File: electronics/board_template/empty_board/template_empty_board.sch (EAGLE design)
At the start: 8 parts, among them IC1 L7805CD2T-TR, J1 GROVE_CONNECTOR2.0_1X4, J2 GROVE_CONNECTOR2.0_1X4

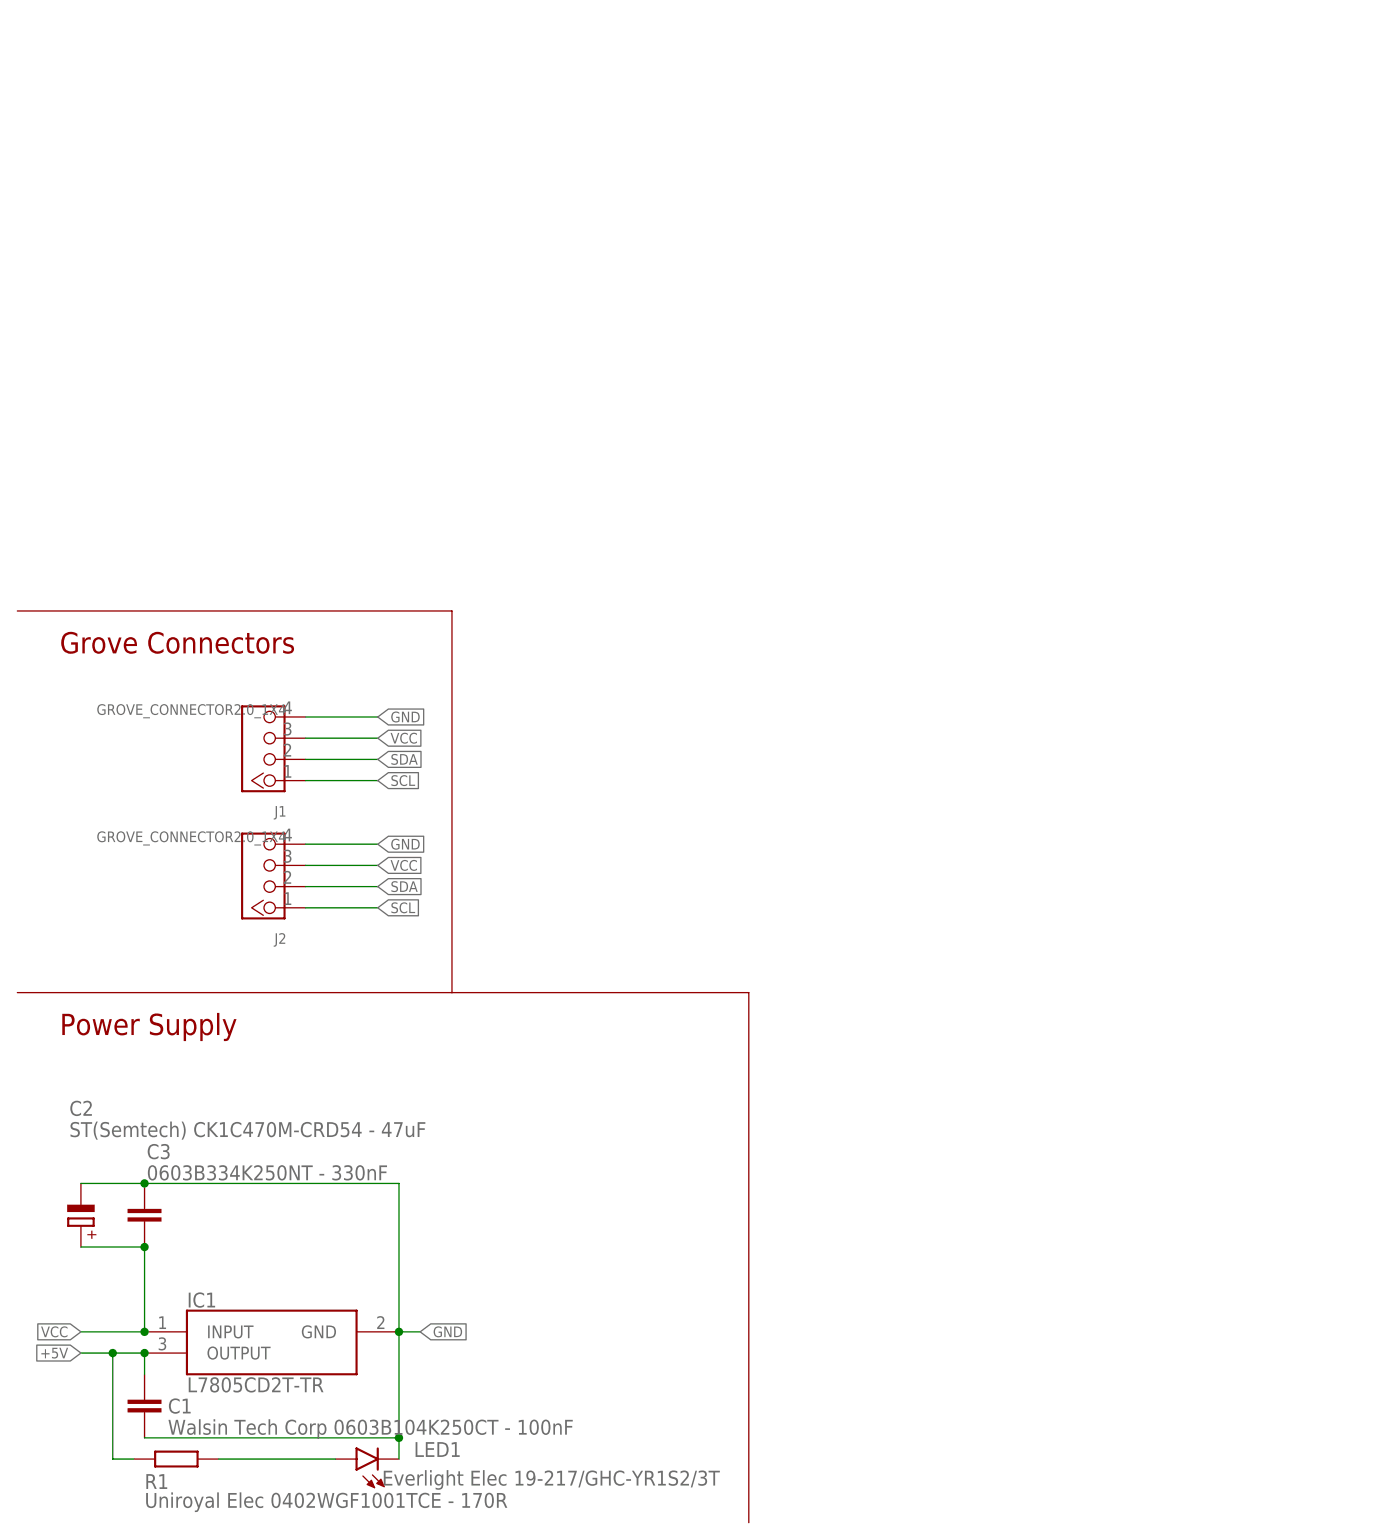
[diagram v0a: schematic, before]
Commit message: Template Empty Board an anderen Linearregler angepasst
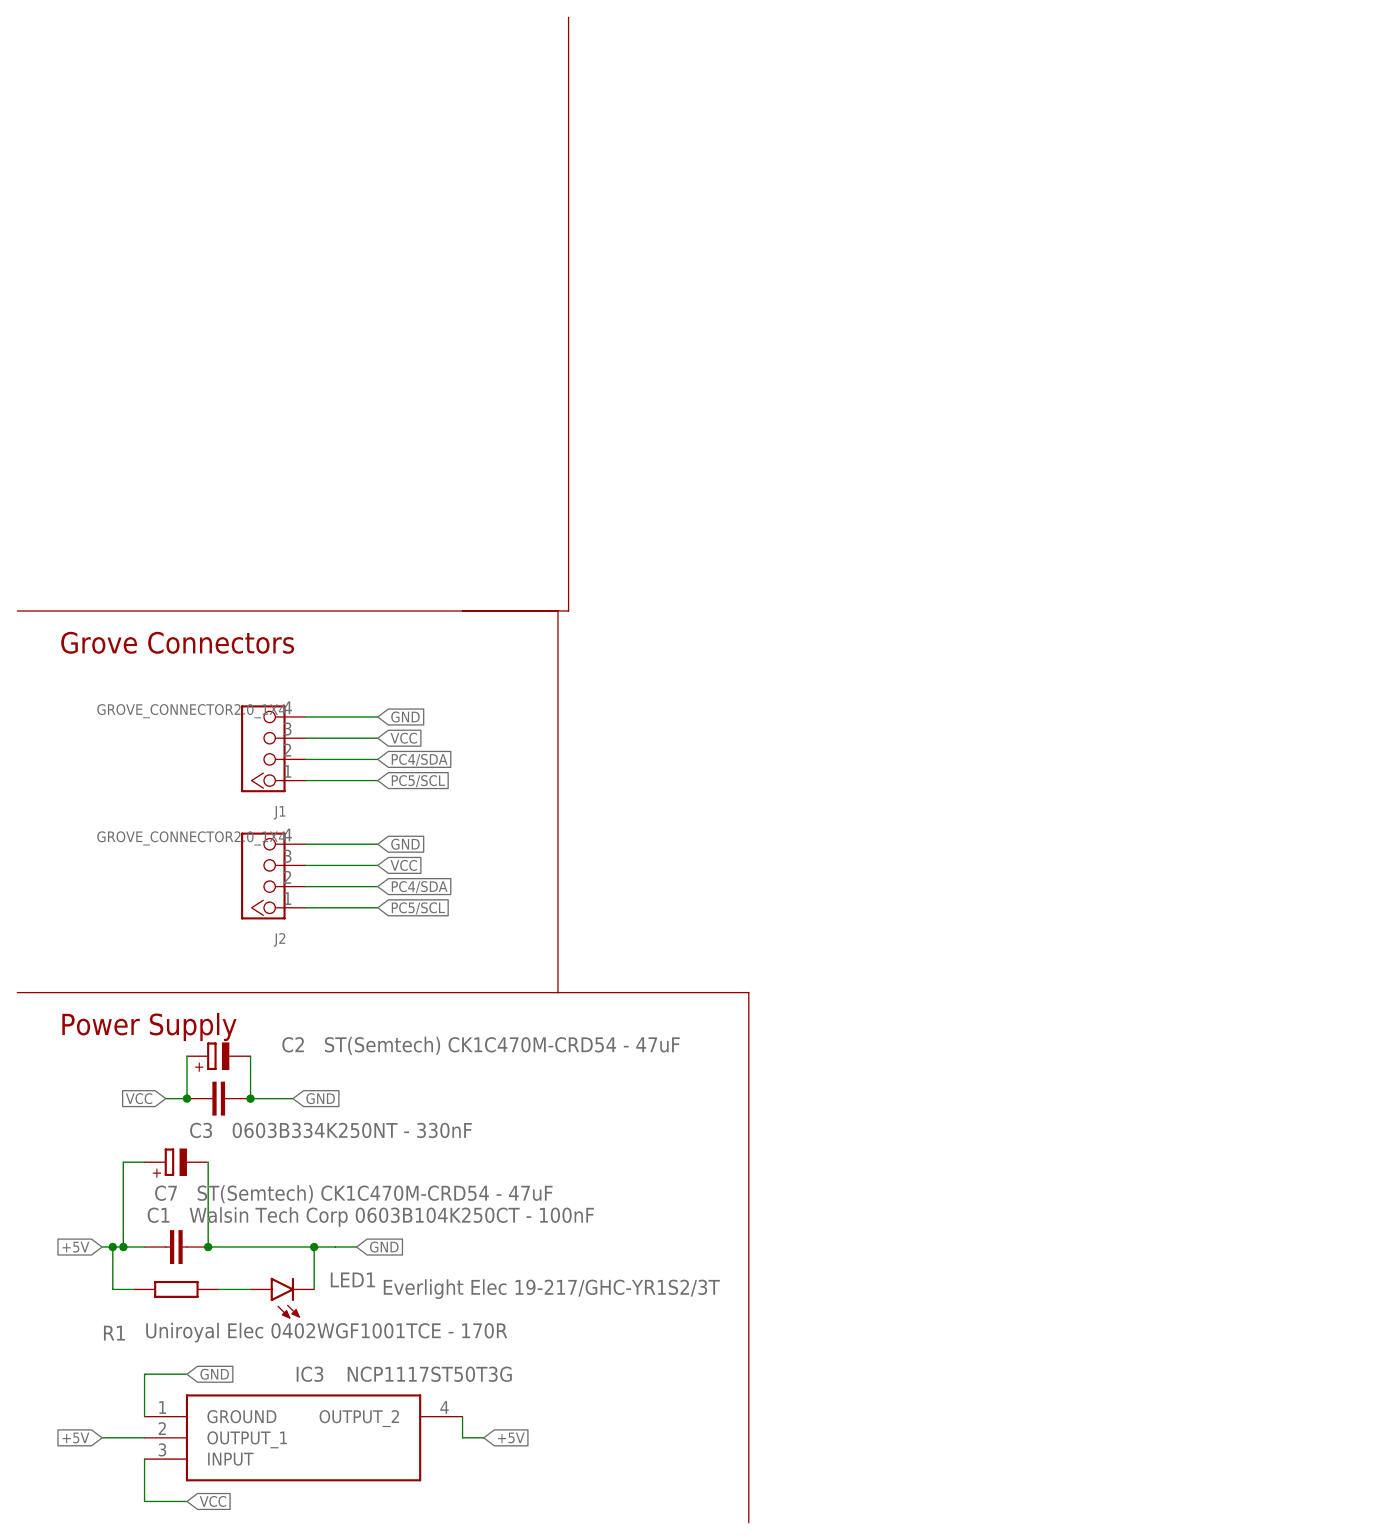
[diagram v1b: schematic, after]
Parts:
- removed IC1: L7805CD2T-TR, morphbot:L7805CD2T-TR
- added C7: ST(Semtech) CK1C470M-CRD54 - 47uF, rcl:CPOL-EUC
- added IC3: NCP1117ST50T3G, samacsys:NCP1117ST50T3G
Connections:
- net SCL renamed PC5/SCL
- net SDA renamed PC4/SDA
- net +5V: now also C7.+, IC3.OUTPUT_1, IC3.OUTPUT_2; no longer IC1.OUTPUT
- net GND: now also C7.-, IC3.GROUND; no longer IC1.GND
- net VCC: now also IC3.INPUT; no longer IC1.INPUT
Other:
- moved on the sheet: C1, C2, C3, LED1, R1

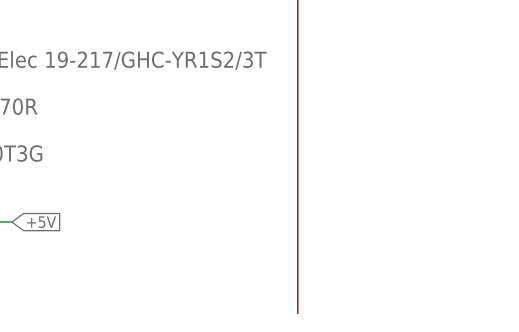
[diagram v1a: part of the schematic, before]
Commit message: Logo hinzugefügt
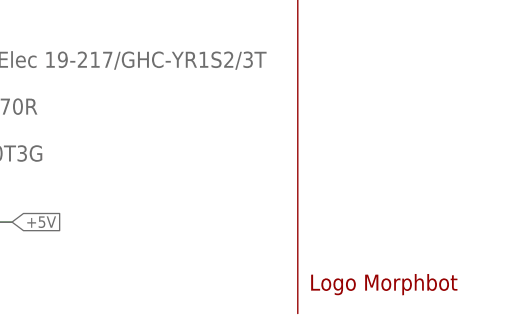
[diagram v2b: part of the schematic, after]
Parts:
- added U$1: LOGO_MORPHBOT5MM, topo-eng:LOGO_MORPHBOT5MM
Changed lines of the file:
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@@
 <layer number="104" name="Name" color="7" fill="1" visible="no" active="yes"/>
 <layer number="116" name="Patch_BOT" color="9" fill="4" visible="no" active="yes"/>
+<layer number="120" name="brd_placement_notes" color="7" fill="1" visible="yes" active="yes"/>
 <layer number="121" name="_tsilk" color="7" fill="1" visible="no" active="yes"/>
 <layer number="122" name="_bsilk" color="7" fill="1" visible="no" active="yes"/>
+<layer number="144" name="DrillLegend" color="7" fill="1" visible="yes" active="yes"/>
+<layer number="145" name="DrillLegend_01-16" color="7" fill="1" visible="yes" active="yes"/>
+<layer number="146" name="DrillLegend_01-20" color="7" fill="1" visible="yes" active="yes"/>
 <layer number="151" name="HeatSink" color="14" fill="1" visible="no" active="no"/>
+<layer number="198" name="BMP198" color="7" fill="1" visible="yes" active="yes"/>
+<layer number="199" name="Contour" color="7" fill="1" visible="yes" active="yes"/>
 <layer number="200" name="200bmp" color="1" fill="10" visible="no" active="no"/>
 <layer number="201" name="201bmp" color="2" fill="1" visible="no" active="no"/>
@@
 <layer number="207" name="207bmp" color="15" fill="10" visible="no" active="no"/>
 <layer number="208" name="208bmp" color="9" fill="10" visible="no" active="yes"/>
+<layer number="209" name="Route9Document" color="7" fill="1" visible="yes" active="yes"/>
+<layer number="210" name="Route10Document" color="7" fill="1" visible="yes" active="yes"/>
+<layer number="211" name="Route11Document" color="7" fill="1" visible="yes" active="yes"/>
+<layer number="212" name="Route12Document" color="7" fill="1" visible="yes" active="yes"/>
+<layer number="213" name="Route13Document" color="7" fill="1" visible="yes" active="yes"/>
+<layer number="214" name="Route14Document" color="7" fill="1" visible="yes" active="yes"/>
+<layer number="215" name="Route15Document" color="7" fill="1" visible="yes" active="yes"/>
+<layer number="216" name="BottomDocument" color="7" fill="1" visible="yes" active="yes"/>
+<layer number="220" name="DimensionDocument" color="7" fill="1" visible="yes" active="yes"/>
+<layer number="221" name="tPlaceDocument" color="7" fill="1" visible="yes" active="yes"/>
+<layer number="222" name="bPlaceDocument" color="7" fill="1" visible="yes" active="yes"/>
+<layer number="225" name="tNamesDocument" color="7" fill="1" visible="yes" active="yes"/>
+<layer number="226" name="bNamesDocument" color="7" fill="1" visible="yes" active="yes"/>
+<layer number="227" name="tValuesDocument" color="7" fill="1" visible="yes" active="yes"/>
+<layer number="228" name="bValuesDocument" color="7" fill="1" visible="yes" active="yes"/>
+<layer number="229" name="tStopDocument" color="7" fill="1" visible="yes" active="yes"/>
+<layer number="230" name="bStopDocument" color="7" fill="1" visible="yes" active="yes"/>
+<layer number="231" name="tCreamDocument" color="7" fill="1" visible="yes" active="yes"/>
+<layer number="232" name="bCreamDocument" color="7" fill="1" visible="yes" active="yes"/>
+<layer number="233" name="tFinishDocument" color="7" fill="1" visible="yes" active="yes"/>
+<layer number="234" name="bFinishDocument" color="7" fill="1" visible="yes" active="yes"/>
+<layer number="235" name="tGlueDocument" color="7" fill="1" visible="yes" active="yes"/>
+<layer number="236" name="bGlueDocument" color="7" fill="1" visible="yes" active="yes"/>
+<layer number="244" name="DrillsDocument" color="7" fill="1" visible="yes" active="yes"/>
+<layer number="245" name="HolesDocument" color="7" fill="1" visible="yes" active="yes"/>
+<layer number="246" name="MillingDocument" color="7" fill="1" visible="yes" active="yes"/>
+<layer number="247" name="MeasuresDocument" color="7" fill="1" visible="yes" active="yes"/>
 <layer number="250" name="Descript" color="3" fill="1" visible="no" active="no"/>
 <layer number="251" name="SMDround" color="12" fill="11" visible="no" active="no"/>
@@
 <part name="IC3" library="samacsys" deviceset="NCP1117ST50T3G" device=""/>
 <part name="C7" library="rcl" library_urn="urn:adsk.eagle:library:334" deviceset="CPOL-EU" device="C" package3d_urn="urn:adsk.eagle:package:23422/2" value="ST(Semtech) CK1C470M-CRD54 - 47uF"/>
+<part name="U$1" library="topo-eng" library_urn="urn:adsk.eagle:library:6646478" deviceset="LOGO_MORPHBOT" device="5MM"/>
 </parts>
 <sheets>
@@
 <attribute name="VALUE" x="21.463" y="38.5826" size="1.778" layer="96"/>
 </instance>
+<instance part="U$1" gate="G$1" x="88.9" y="2.54" smashed="yes"/>
 </instances>
 <busses>

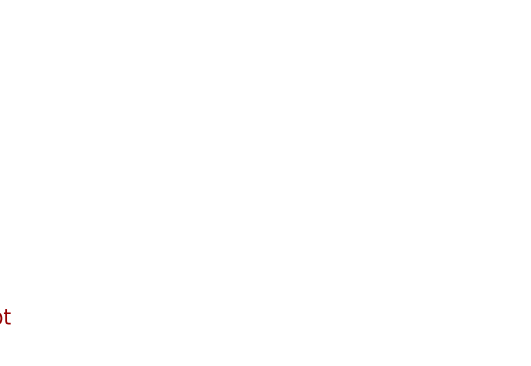
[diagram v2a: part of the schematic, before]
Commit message: Fiducials eingefügt
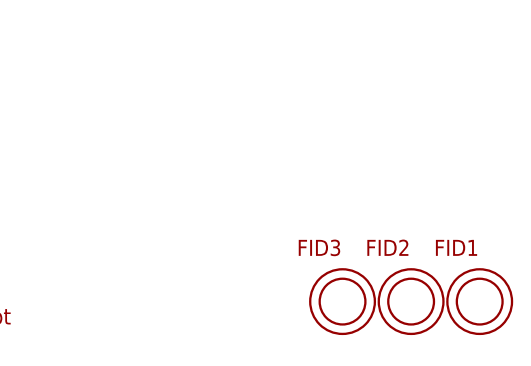
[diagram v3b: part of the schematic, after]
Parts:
- added FID1, FID2, FID3: OPEN-PNP-FIDUCIAL, topo-eng:OPEN-PNP-FIDUCIAL
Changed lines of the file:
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@@
 <part name="C7" library="rcl" library_urn="urn:adsk.eagle:library:334" deviceset="CPOL-EU" device="C" package3d_urn="urn:adsk.eagle:package:23422/2" value="ST(Semtech) CK1C470M-CRD54 - 47uF"/>
 <part name="U$1" library="topo-eng" library_urn="urn:adsk.eagle:library:6646478" deviceset="LOGO_MORPHBOT" device="5MM"/>
+<part name="FID1" library="topo-eng" library_urn="urn:adsk.eagle:library:6646478" deviceset="OPEN-PNP-FIDUCIAL" device=""/>
+<part name="FID2" library="topo-eng" library_urn="urn:adsk.eagle:library:6646478" deviceset="OPEN-PNP-FIDUCIAL" device=""/>
+<part name="FID3" library="topo-eng" library_urn="urn:adsk.eagle:library:6646478" deviceset="OPEN-PNP-FIDUCIAL" device=""/>
 </parts>
 <sheets>
@@
 </instance>
 <instance part="U$1" gate="G$1" x="88.9" y="2.54" smashed="yes"/>
+<instance part="FID1" gate="FID$1" x="157.48" y="5.08" smashed="yes">
+<attribute name="NAME" x="152.4" y="10.16" size="1.778" layer="94"/>
+</instance>
+<instance part="FID2" gate="FID$1" x="149.86" y="5.08" smashed="yes">
+<attribute name="NAME" x="144.78" y="10.16" size="1.778" layer="94"/>
+</instance>
+<instance part="FID3" gate="FID$1" x="142.24" y="5.08" smashed="yes">
+<attribute name="NAME" x="137.16" y="10.16" size="1.778" layer="94"/>
+</instance>
 </instances>
 <busses>
